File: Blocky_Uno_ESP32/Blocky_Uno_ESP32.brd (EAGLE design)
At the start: 68.7 x 53.5 mm, 54 parts, among them Q2 S8050, Q3 DMG3415U, Q6 S8050, U1 ESP-WROOM-32NARROW, U2 AP2112-3.3, U5 MCP73831T-2ACI/OT, U6 CH340C, X1 JSTPH

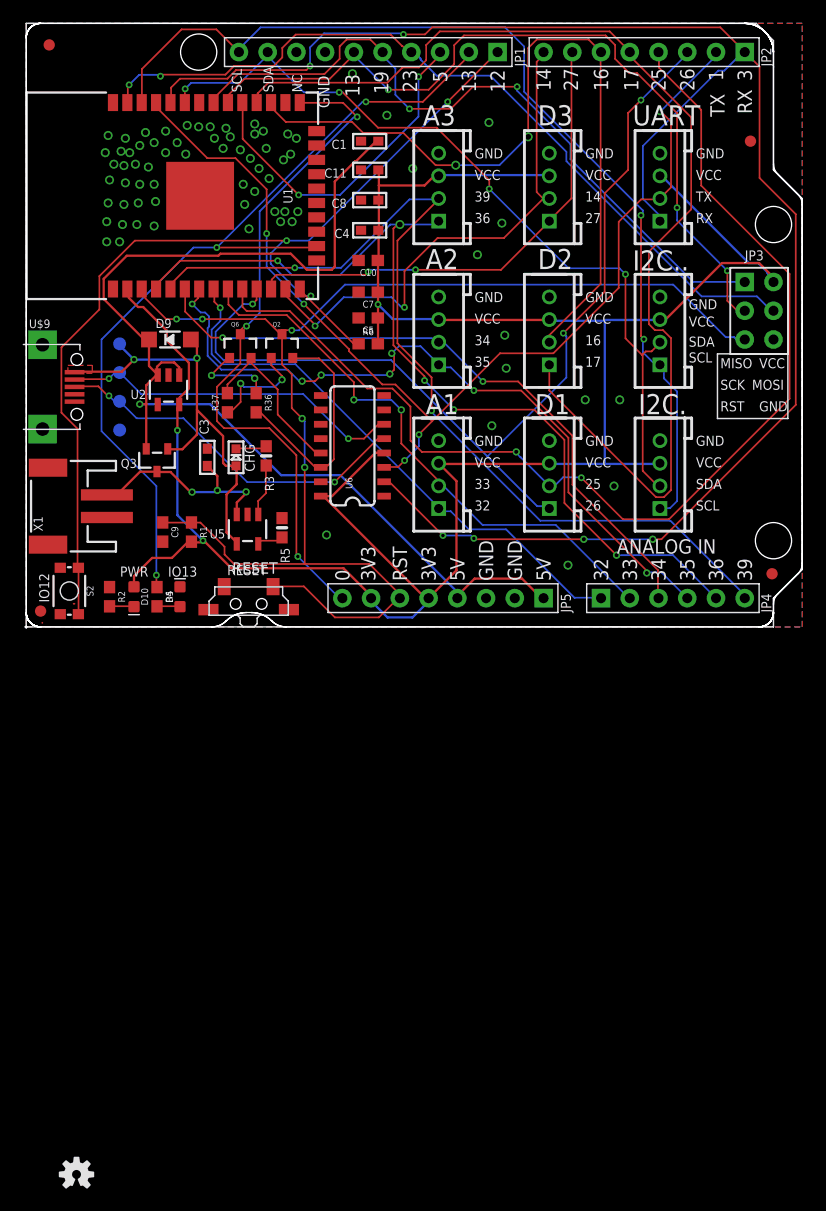
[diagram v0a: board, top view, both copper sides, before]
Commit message: Fix error with GND trace
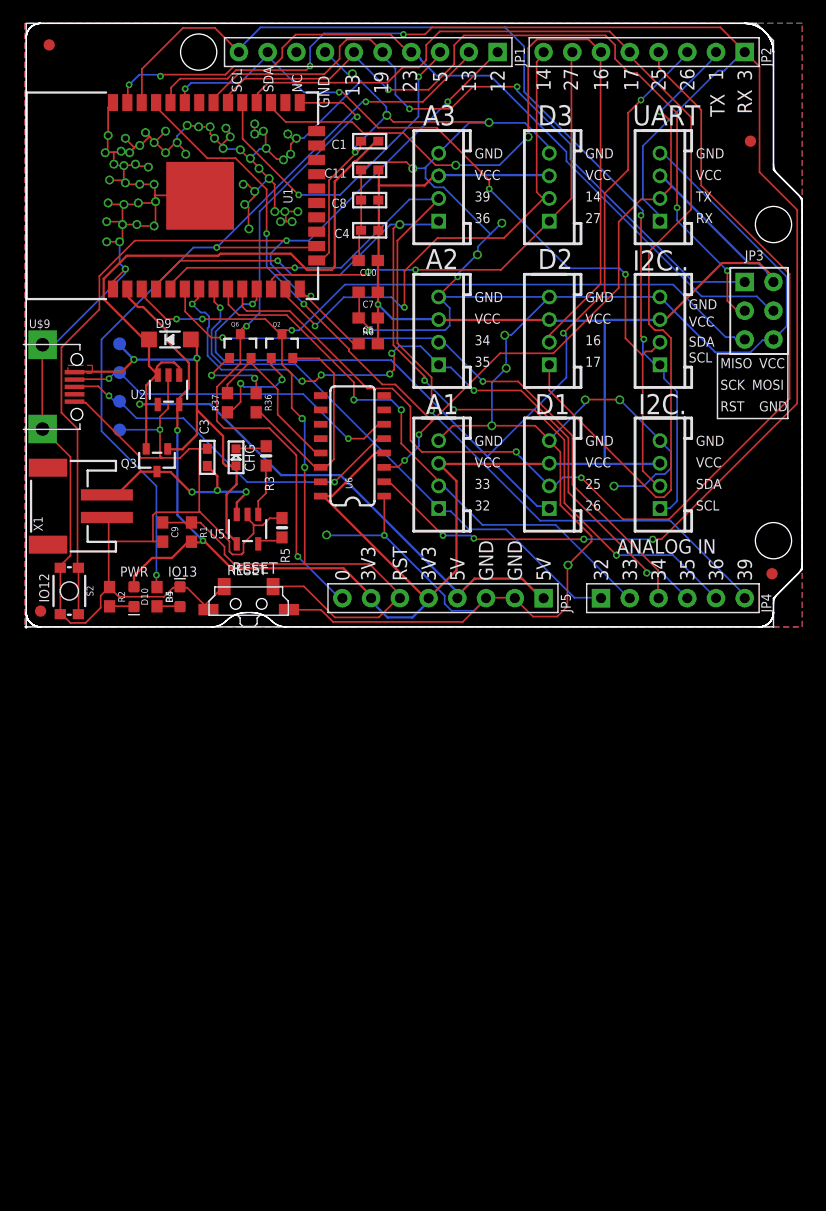
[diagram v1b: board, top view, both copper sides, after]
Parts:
- removed LOGO1: REVISION, SparkFun-Aesthetics:REVISION
- removed LOGO3: OSHW-LOGOS, SparkFun-Aesthetics:OSHW-LOGO-S
- FRAME1: value FRAME-LETTER -> (none); device SparkFun-Aesthetics:CREATIVE_COMMONS -> SparkFun-Aesthetics:DUMMY
- moved FRAME1 33.4 mm to (-6.35, -1.02)
- moved U$4 8.23 mm to (20.6, 17.4)
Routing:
- net GND: track 0.32 -> 477.2 mm, vias 72 -> 78
